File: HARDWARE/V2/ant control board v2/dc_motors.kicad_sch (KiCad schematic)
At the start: 12 parts, among them J3 M1, J4 M2, J5 M3, U3 DRV8837, U4 DRV8837, U5 DRV8837

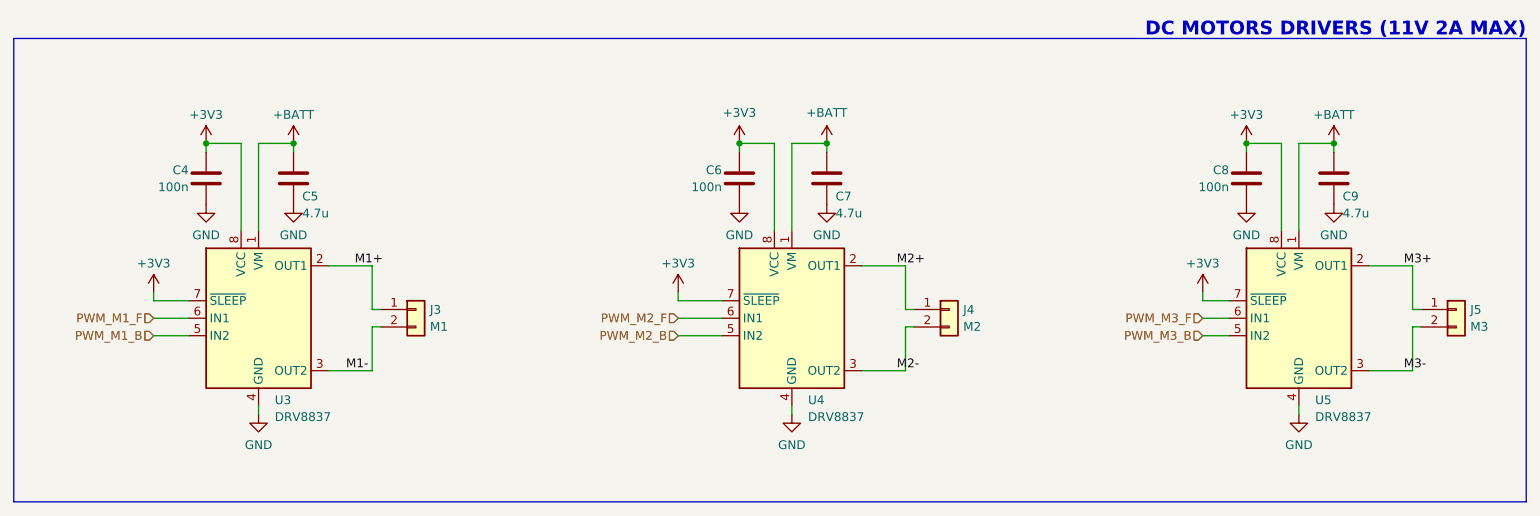
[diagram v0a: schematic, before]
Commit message: layout 2.0 facv2 done
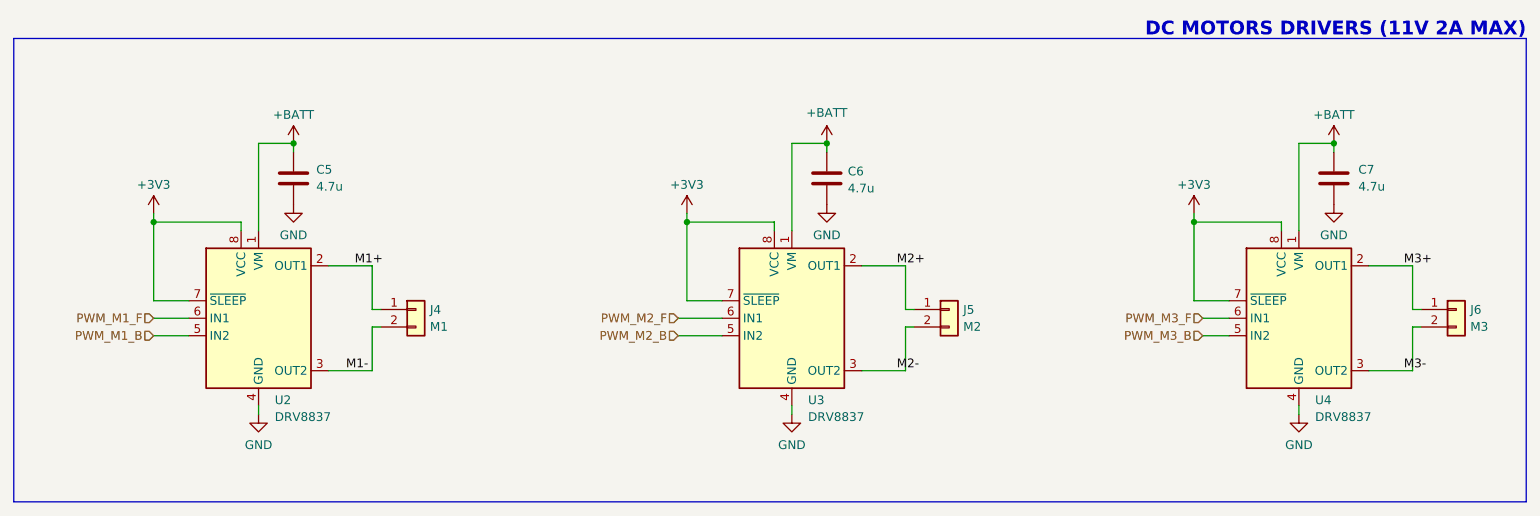
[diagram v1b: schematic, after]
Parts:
- removed C4, C6, C8: 100n, Capacitor_SMD:C_0603_1608Metric, symbol Device:C
- C5: footprint Capacitor_SMD:C_0603_1608Metric -> Capacitor_SMD:C_0402_1005Metric
- C6: renamed from C7; footprint Capacitor_SMD:C_0603_1608Metric -> Capacitor_SMD:C_0402_1005Metric
- C7: renamed from C9; footprint Capacitor_SMD:C_0603_1608Metric -> Capacitor_SMD:C_0402_1005Metric
- J4: renamed from J3; footprint _MY_connectors:Pad 02x01 -> _MY_connectors:01x02_TH_pad_renforced
- J5: renamed from J4; footprint _MY_connectors:Pad 02x01 -> _MY_connectors:01x02_TH_pad_renforced
- J6: renamed from J5; footprint _MY_connectors:Pad 02x01 -> _MY_connectors:01x02_TH_pad_renforced
- U2: renamed from U3; LCSC (none) -> C39159
- U3: renamed from U4; LCSC (none) -> C39159
- U4: renamed from U5; LCSC (none) -> C39159
